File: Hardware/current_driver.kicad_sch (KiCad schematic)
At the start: 2 parts, among them U1 30mA const current led driver

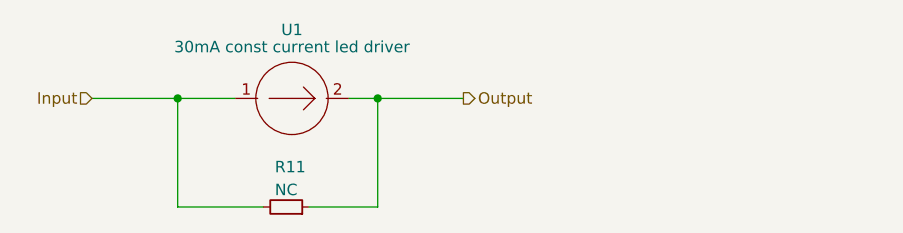
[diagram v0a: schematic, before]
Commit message: Dodano esd protection, zmieniono komponenty, poprawiono schemat itp
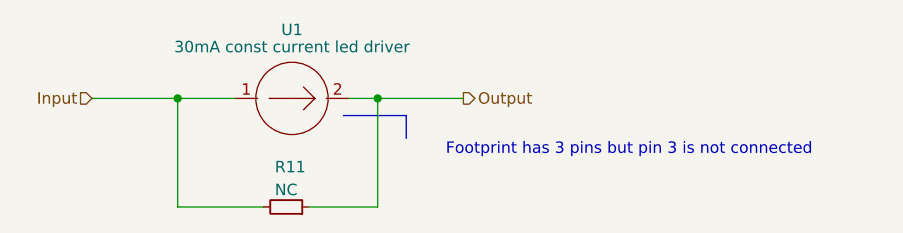
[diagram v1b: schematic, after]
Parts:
- U1: footprint Include:DIO_1-13_DIO-L -> Diode_SMD:D_PowerDI-123; mouser (none) -> https://www.mouser.pl/ProductDetail/Diodes-Incorporated/AL5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
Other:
- note added: "Footprint has 3 pins but pin 3 is not connected"
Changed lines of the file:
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@@
 	(generator_version "9.0")
 	(paper "A4")
+	(text "Footprint has 3 pins but pin 3 is not connected"
+		(exclude_from_sim no)
+		(at 148.59 100.965 0)
+		(effects
+			(font
+				(size 1.27 1.27)
+			)
+		)
+	)
 	(junction
 		(at 120.65 95.25)
@@
 		)
 	)
+	(polyline
+		(pts
+			(xy 123.825 99.695) (xy 123.825 97.155)
+		)
+		(stroke
+			(width 0)
+			(type default)
+		)
+	)
 	(wire
 		(pts
@@
 		(pts
 			(xy 107.95 107.315) (xy 98.425 107.315)
+		)
+		(stroke
+			(width 0)
+			(type default)
+		)
+	)
+	(polyline
+		(pts
+			(xy 116.84 97.155) (xy 123.825 97.155)
 		)
 		(stroke
@@
 			)
 		)
-		(property "Footprint" "Include:DIO_1-13_DIO-L"
+		(property "Footprint" "Diode_SMD:D_PowerDI-123"
 			(at 111.125 95.25 0)
 			(effects
@@
 			)
 		)
-		(property "Datasheet" "https://www.mouser.pl/ProductDetail/Diodes-Incorporated/AL5890-30P1-13?qs=sGAEpiMZZMtnFuLo2AlFPiAYlxlJUBTwXUu5s31upKx%252BoZPguTR9ww%3D%3D"
+		(property "Datasheet" "https://www.diodes.com/assets/Datasheets/AL5809Q.pdf"
 			(at 111.125 95.25 0)
 			(effects
@@
 			(at 111.125 95.25 0)
 			(effects
+				(font
+					(size 1.27 1.27)
+				)
+				(hide yes)
+			)
+		)
+		(property "mouser" "https://www.mouser.pl/ProductDetail/Diodes-Incorporated/AL5809-30QP1-7?qs=icAhCOE9TbioChqKyh2OuA%3D%3D"
+			(at 111.125 95.25 0)
+			(effects
